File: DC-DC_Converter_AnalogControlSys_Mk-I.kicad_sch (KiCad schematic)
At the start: 3 parts, among them Q1 OSP120N04T, U1 TL054CN, U2 TL052AIP

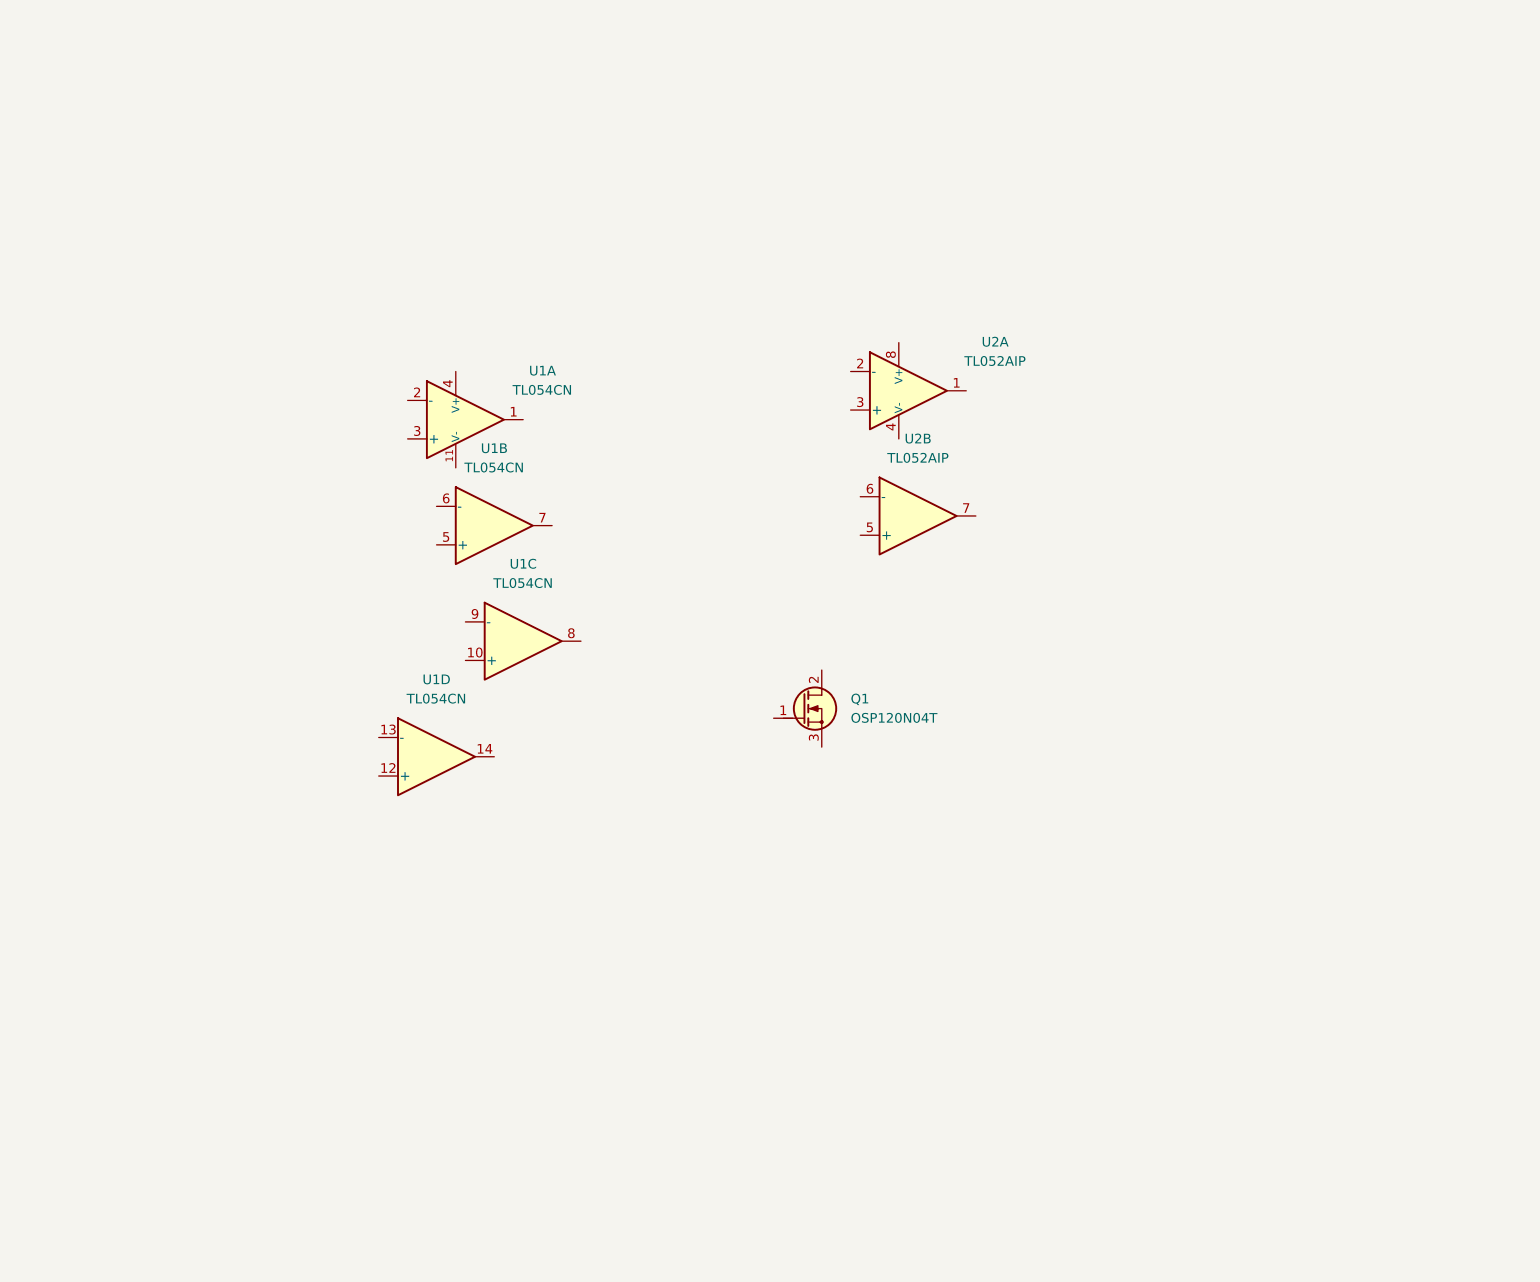
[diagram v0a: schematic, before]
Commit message: ADDED potentiometer footprint. ADDED layout of PI controller and PWM generator. TODO determine clock source, then assign component values and LCSC numbers.
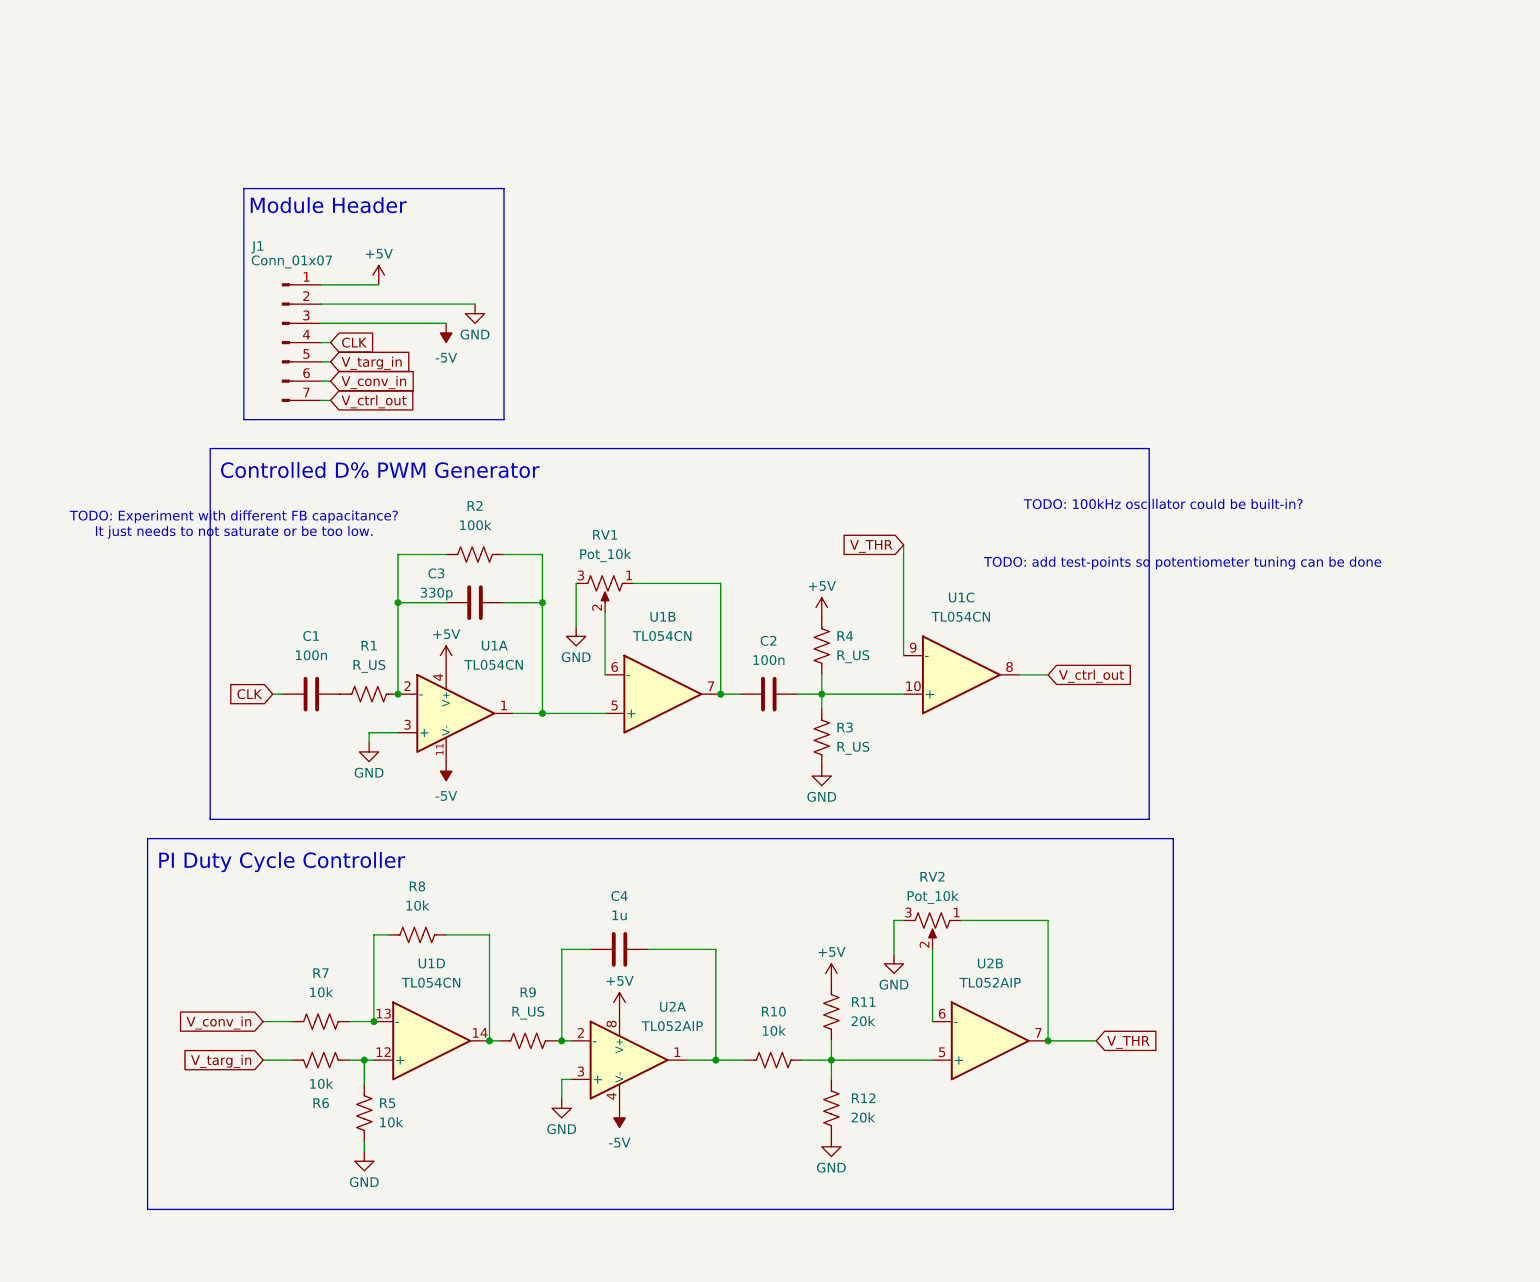
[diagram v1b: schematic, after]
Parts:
- removed Q1: OSP120N04T, Package_TO_SOT_THT:TO-220-3_Vertical, symbol DCDCCACS1:OSP120N04T
- added C1, C2: 100n, symbol Device:C
- added C3: 330p, symbol Device:C
- added C4: 1u, symbol Device:C
- added J1: Conn_01x07, symbol Connector:Conn_01x07_Pin
- added R1, R3, R4, R9: R_US, symbol Device:R_US
- added R10, R5, R6, R7, R8: 10k, symbol Device:R_US
- added R11, R12: 20k, symbol Device:R_US
- added R2: 100k, symbol Device:R_US
- added RV1, RV2: Pot_10k, DCDCCACS1_footprints:JIERR 3362P Pot, symbol Device:R_Potentiometer_US
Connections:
- net at U2.1: now also C4.2, R10.2
- net at U2.2 (-): now also C4.1, R9.1
- net GND: now reaches U2.3 (+)
- net GND: now also U1.3 (+), J1.2 (Pin_2), R12.2, R3.1, R5.1, RV1.3, RV2.3
- net -5V: now reaches U2.4 (V-)
- net -5V: now also U1.11 (V-), J1.3 (Pin_3)
- net +5V: now reaches U2.8 (V+)
- net +5V: now also U1.4 (V+), J1.1 (Pin_1), R11.1, R4.2
- net at U1.12 (+): now also R5.2, R6.2
- net at U1.13 (-): now also R7.1, R8.2
- net at U1.14: now also R8.1, R9.2
- net at U1.1: now also U1.5 (+), C3.2, R2.2
- net at U1.2 (-): now also C3.1, R1.2, R2.1
- net at U2.5 (+): now also R10.1, R11.2, R12.1
- net at U2.6 (-): now also RV2.2
- net V_THR: now reaches U2.7
- net V_THR: now also U1.9 (-), RV2.1
- net at U1.10 (+): now also C2.2, R3.2, R4.1
- net V_ctrl_out: now reaches U1.8
- net V_ctrl_out: now also J1.7 (Pin_7)
- net at U1.6 (-): now also RV1.2
- net at U1.7: now also C2.1, RV1.1
- new net: C1.2, R1.1
- new net CLK: C1.1, J1.4 (Pin_4)
- new net V_conv_in: J1.6 (Pin_6), R7.2
- new net V_targ_in: J1.5 (Pin_5), R6.1
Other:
- note added: "Controlled D% PWM Generator"
- note added: "Module Header"
- note added: "PI Duty Cycle Controller"
- note added: "TODO: 100kHz oscillator could be built-in?"
- note added: "TODO: Experiment with different FB capacitance? It just needs to not saturate or be too low."
- note added: "TODO: add test-points so potentiometer tuning can be done"
- company: (none) -> Zachary Hobbs
- title: (none) -> DC-DC Converter Analog Control System Mk-I
- moved on the sheet: U1A, U1B, U1C, U1D, U2A, U2B

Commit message: FIXED analog control system to work much better and matches the LTspice sim. ADDED optionally-usable 10W 5x boost converter module. TODO find and assign LCSC part numbers and footprints, before beginning PCB.
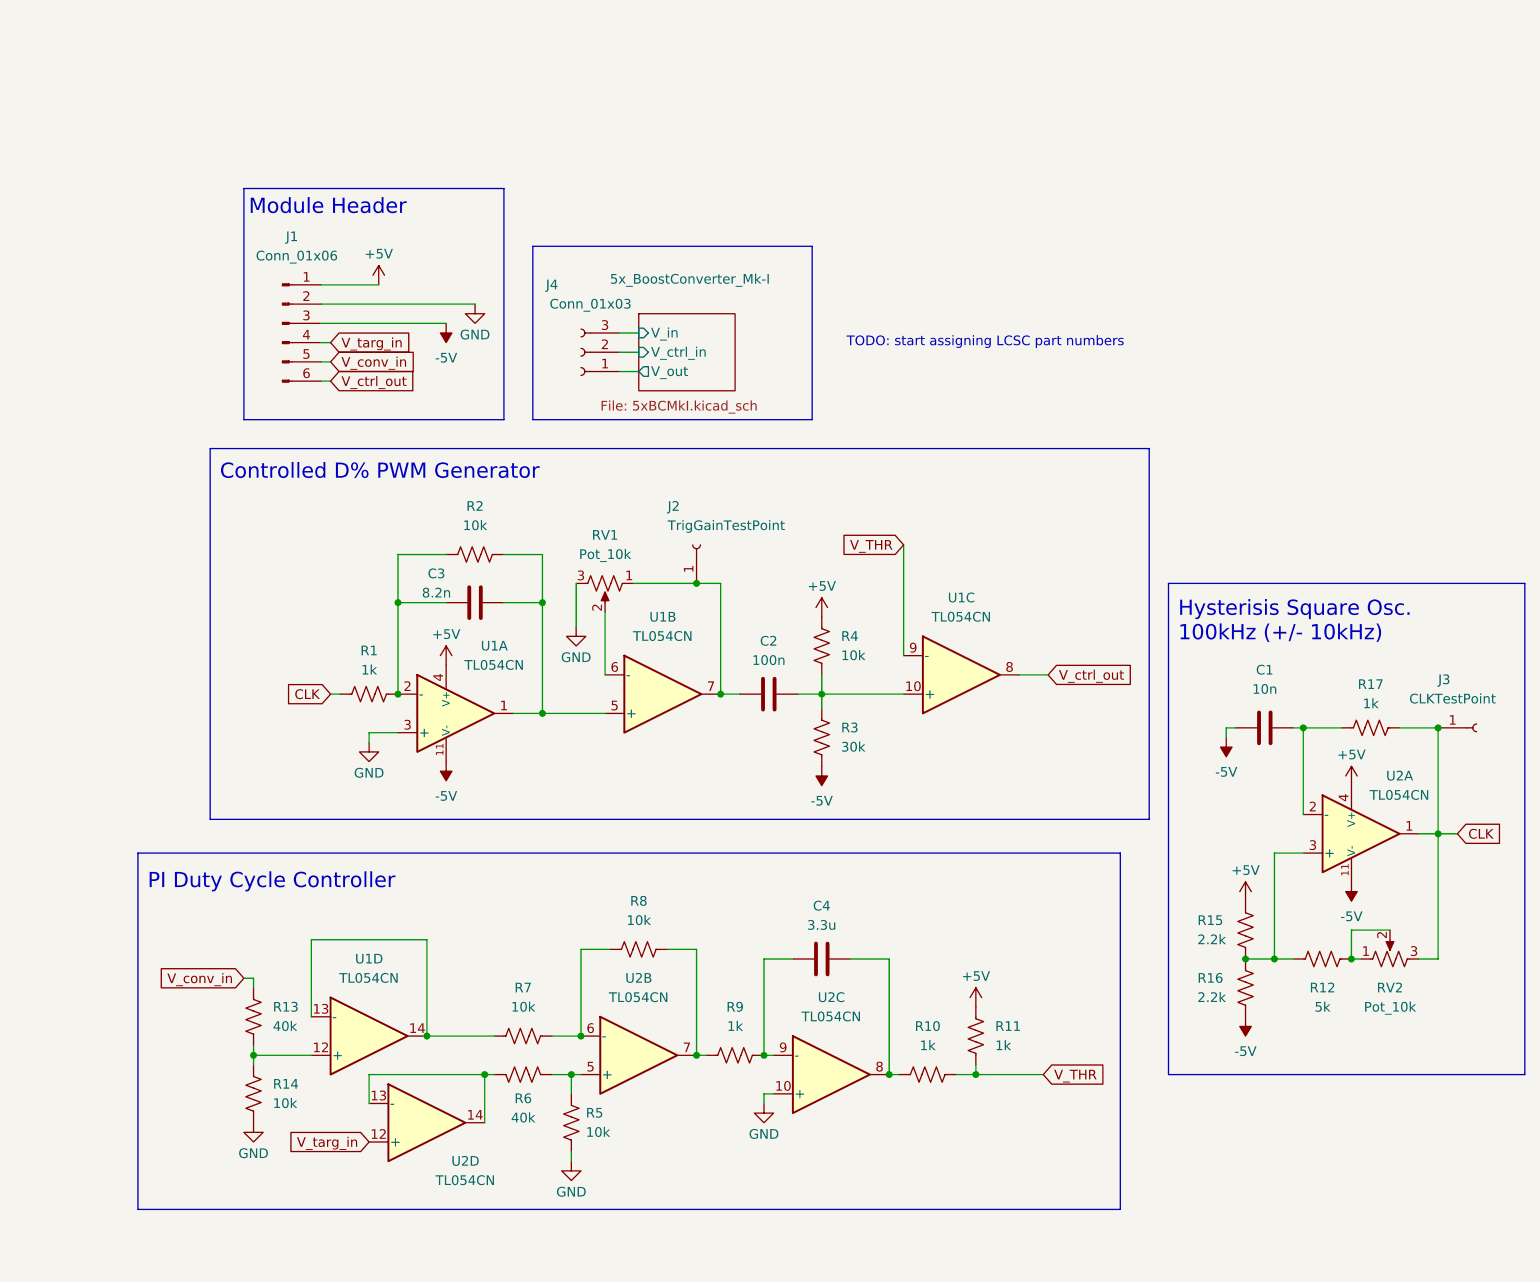
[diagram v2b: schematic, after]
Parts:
- removed J1: Conn_01x07, symbol Connector:Conn_01x07_Pin
- removed U2: TL052AIP, PCM_Package_DIP_AKL:DIP-8_W7.62mm_LongPads, symbol PCM_Amplifier_Operational_AKL:TL052AIP
- added J1: Conn_01x06, symbol Connector:Conn_01x06_Pin
- added J2: TrigGainTestPoint, Connector_PinHeader_2.54mm:PinHeader_1x01_P2.54mm_Vertical, symbol Connector:Conn_01x01_Socket
- added J3: CLKTestPoint, Connector_PinHeader_2.54mm:PinHeader_1x01_P2.54mm_Vertical, symbol Connector:Conn_01x01_Socket
- added J4: Conn_01x03, symbol Connector:Conn_01x03_Socket
- added R13: 40k, symbol Device:R_US
- added R14: 10k, symbol Device:R_US
- added R15, R16: 2.2k, symbol Device:R_US
- added R17: 1k, symbol Device:R_US
- added U2: TL054CN, PCM_Package_DIP_AKL:DIP-14_W7.62mm_LongPads, symbol PCM_Amplifier_Operational_AKL:TL054CN
- C1: value 100n -> 10n
- C3: value 330p -> 8.2n
- C4: value 1u -> 3.3u
- R1, R9: value R_US -> 1k
- R10: value 10k -> 1k
- R11: value 20k -> 1k
- R12: value 20k -> 5k
- R2: value 100k -> 10k
- R3: value R_US -> 30k
- R4: value R_US -> 10k
- R6: value 10k -> 40k
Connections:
- net +5V: now also J1.1 (Pin_1), R15.2, U2.4 (V+)
- net -5V: now also C1.1, R3.1, J1.3 (Pin_3), R16.1, U2.11 (V-)
- net CLK: now also R1.1, RV2.3, J3.1 (Pin_1), R17.2, U2.1; no longer C1.1
- net GND: now also J1.2 (Pin_2), R14.2, U2.10 (+); no longer R12.2, R3.1, RV2.3
- net V_THR: now also R10.1, R11.2; no longer RV2.1
- net V_conv_in: now also J1.5 (Pin_5), R13.1; no longer R7.2
- net V_ctrl_out: now also J1.6 (Pin_6)
- net V_targ_in: now also J1.4 (Pin_4), U2.12 (+); no longer R6.1
- net at RV2.2: now also R12.2, RV2.1
- net at R5.2, R6.2: now also U2.5 (+); no longer U1.12 (+)
- net at C4.2, R10.2: now also U2.8
- net at C4.1, R9.1: now also U2.9 (-)
- net at R7.1, R8.2: now also U2.6 (-); no longer U1.13 (-)
- net at R8.1, R9.2: now also U2.7; no longer U1.14
- net at C1.2: now also R17.1, U2.2 (-); no longer R1.1
- net at C2.1, RV1.1, U1.7: now also J2.1 (Pin_1)
- new net: R13.2, R14.1, U1.12 (+)
- new net: R7.2, U1.13 (-), U1.14
- new net: R12.1, R15.1, R16.2, U2.3 (+)
- new net: R6.1, U2.13 (-), U2.14
- new net 5x_BoostConverter_Mk-I/V_ctrl_in: J4.2 (Pin_2)
- new net 5x_BoostConverter_Mk-I/V_in: J4.3 (Pin_3)
- new net 5x_BoostConverter_Mk-I/V_out: J4.1 (Pin_1)
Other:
- added sheet 5x_BoostConverter_Mk-I (5xBCMkI.kicad_sch)
- note added: "Hysterisis Square Osc. 100kHz (+/- 10kHz)"
- note added: "TODO: start assigning LCSC part numbers"
- note removed: "TODO: 100kHz oscillator could be built-in?"
- note removed: "TODO: Experiment with different FB capacitance? It just needs to not saturate or be too low."
- note removed: "TODO: add test-points so potentiometer tuning can be done"
- moved on the sheet: C1, C4, R10, R11, R5, R6, R7, R8, R9, RV2, U1D

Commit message: FIXED schematic to match simulation. TODO assign LCSC part numbers.
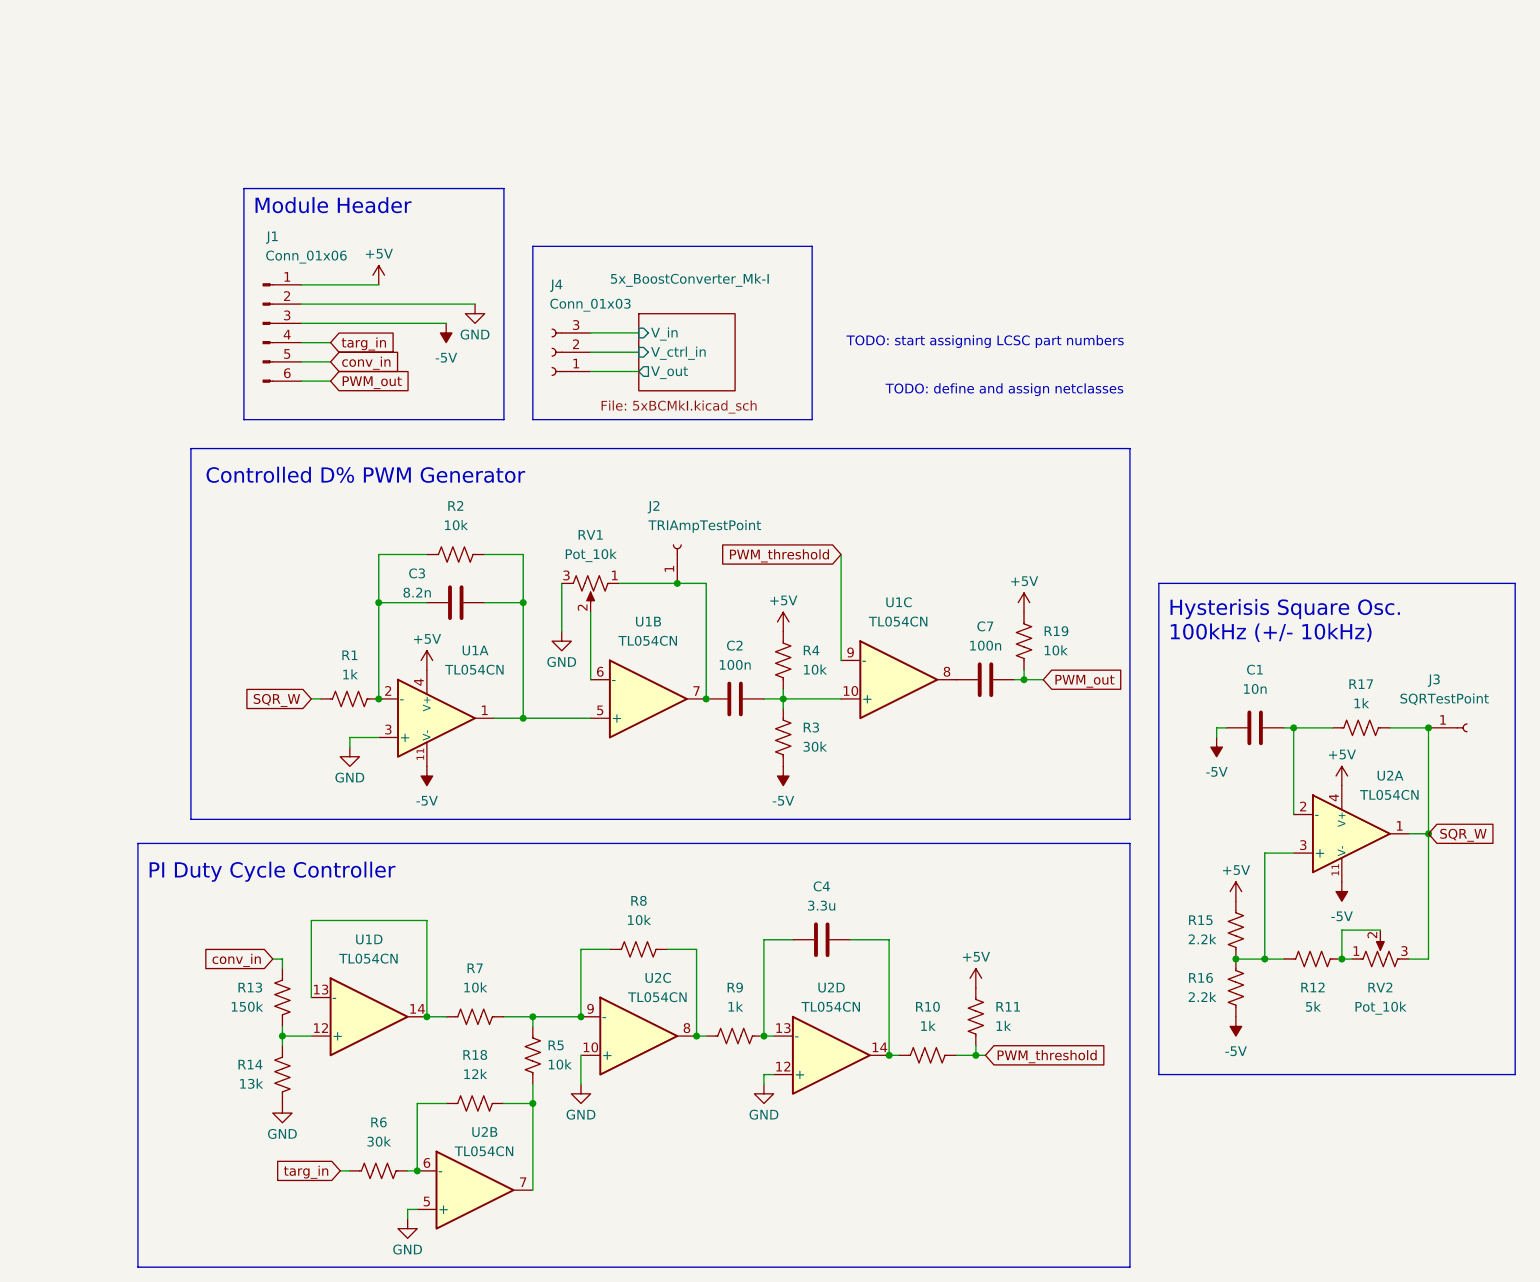
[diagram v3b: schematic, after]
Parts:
- added C7: 100n, symbol Device:C
- added R18: 12k, symbol Device:R_US
- added R19: 10k, symbol Device:R_US
- J2: value TrigGainTestPoint -> TRIAmpTestPoint
- J3: value CLKTestPoint -> SQRTestPoint
- R13: value 40k -> 150k
- R14: value 10k -> 13k
- R6: value 40k -> 30k
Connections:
- net +5V: now also R19.2
- net GND: now also R14.1, U2.12 (+), U2.5 (+); no longer R14.2, R5.1
- net at R7.1, R8.2: now also R5.2, U2.9 (-); no longer U2.6 (-)
- net at R8.1, R9.2: now also U2.8; no longer U2.7
- net at R13.2, U1.12 (+): now also R14.2; no longer R14.1
- net at C4.2, R10.2: now also U2.14; no longer U2.8
- net at C4.1, R9.1: now also U2.13 (-); no longer U2.9 (-)
- net CLK renamed SQR_W
- net V_THR renamed PWM_threshold
- net V_conv_in renamed conv_in
- net V_ctrl_out: no longer names the net of U1.8
- net V_ctrl_out: now also C7.1; no longer J1.6 (Pin_6)
- net V_targ_in renamed targ_in
- net targ_in: now also R6.2; no longer U2.12 (+)
- new net: R18.1, R5.1, U2.7
- new net: R18.2, R6.1, U2.6 (-)
- new net PWM_out: C7.2, J1.6 (Pin_6), R19.1
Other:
- note added: "TODO: define and assign netclasses"
- moved on the sheet: C1, C2, C3, C4, J1, J2, J3, J4, R1, R10, R11, R12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
